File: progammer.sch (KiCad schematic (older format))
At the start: 75 parts, among them J5 USB_B_Micro, U1 ICE40HX4K-TQ144, U11 SN74LVC2T45DCUR, U13 SN74AXC4T245PWR, U14 MIC5365-3.3YC5, U16 SN74LVC2T45DCUR, U17 SN74LVC2T45DCUR, U18 SN74LVC2T45DCUR, U19 SN74LVC2T45DCUR, U3 93LCxxBT-I_OT, U4 FT2232H, U5 IS25LP080D, Y1 ECS-3225S33-120-FN-TR

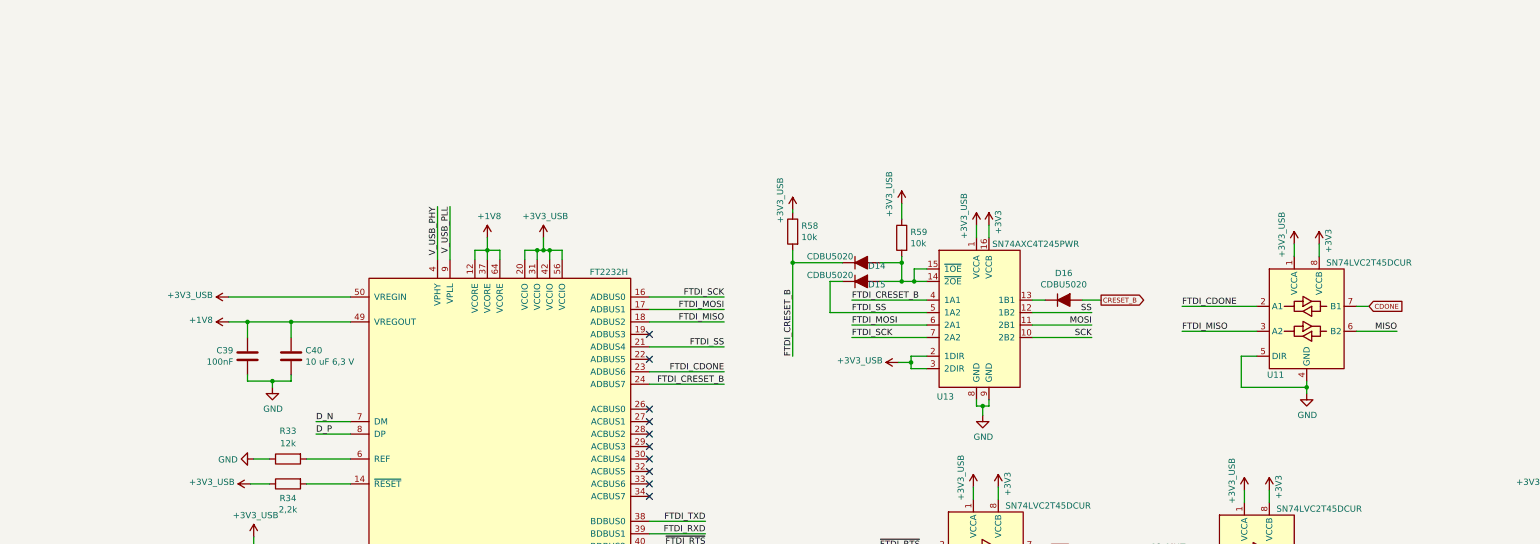
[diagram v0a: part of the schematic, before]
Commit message: Changed power isolation to usb power to use an open drain translator for the reset signals. Continued on routing
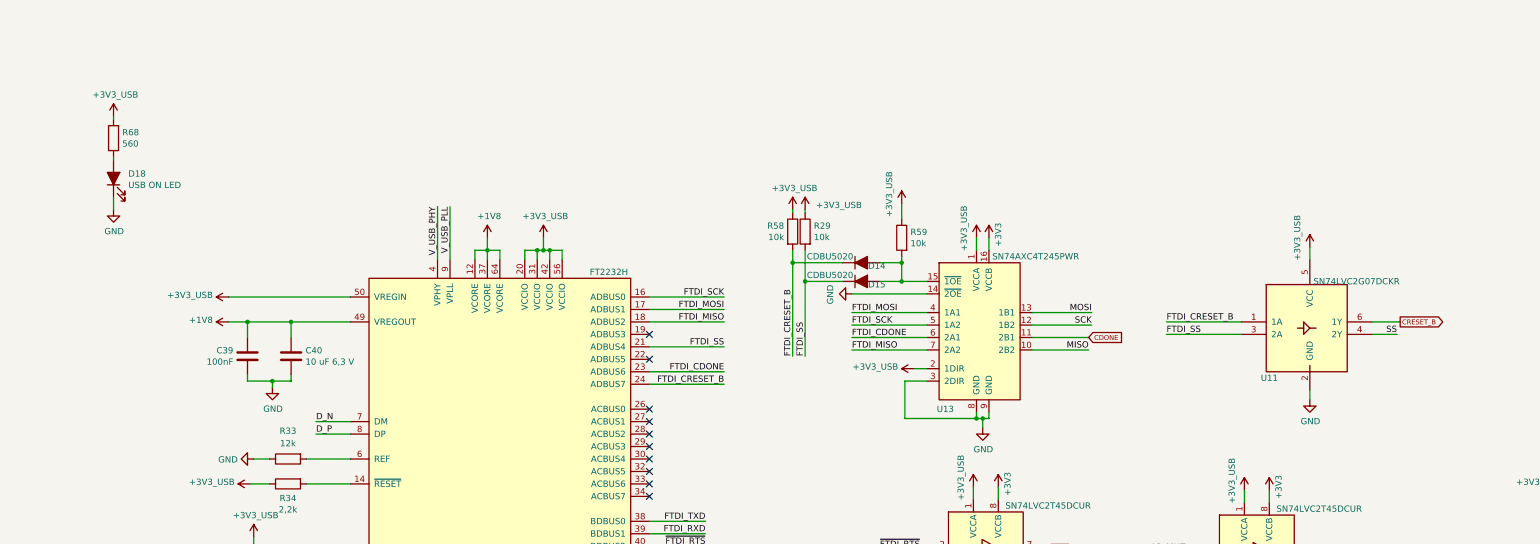
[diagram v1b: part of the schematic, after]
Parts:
- removed D16: CDBU5020, Diode_SMD:D_0603_1608Metric, symbol Device:D_ALT
- removed U11: SN74LVC2T45DCUR, Package_SO:VSSOP-8_2.4x2.1mm_P0.5mm, symbol Logic_LevelTranslator:SN74LVC2T45DCUR
- added D18: USB ON LED, LED_SMD:LED_0603_1608Metric, symbol Device:LED_ALT
- added R29: 10k, Resistor_SMD:R_0603_1608Metric, symbol Device:R
- added R68: 560, Resistor_SMD:R_0603_1608Metric, symbol Device:R
- added U11: SN74LVC2G07DCKR, Package_TO_SOT_SMD:SOT-363_SC-70-6, symbol SN74LVC2G07:SN74LVC2G07DCKR
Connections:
- net +3V3_FTDI: now also R29.1, R68.1, U11.5 (VCC); no longer U13.3 (2DIR)
- net CDONE: now also U13.11 (2B1)
- net CRESET_B: now also U11.6 (1Y)
- net FTDI_CDONE: now also U13.6 (2A1)
- net FTDI_CRESET_B: now also U11.1 (1A); no longer U13.4 (1A1)
- net FTDI_MISO: now also U13.7 (2A2)
- net FTDI_MOSI: now also U13.4 (1A1); no longer U13.6 (2A1)
- net FTDI_SCK: now also U13.5 (1A2); no longer U13.7 (2A2)
- net FTDI_SS: now also R29.2, U11.3 (2A); no longer U13.5 (1A2)
- net GND: now also U13.14 (~2OE~), U13.3 (2DIR), D18.1 (K), U11.2 (GND)
- net MISO: now also U13.10 (2B2)
- net MOSI: now also U13.13 (1B1); no longer U13.11 (2B1)
- net SCK: now also U13.12 (1B2); no longer U13.10 (2B2)
- net SS: now also U11.4 (2Y); no longer U13.12 (1B2)
- net at D14.2 (A), D15.2 (A), R59.2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: no longer U13.14 (~2OE~)
- new net: D18.2 (A), R68.2
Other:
- moved on the sheet: U13

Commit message: Routing mostly done
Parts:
- removed C80: 100nF, Capacitor_SMD:C_0603_1608Metric, symbol Device:C
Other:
- moved on the sheet: C79
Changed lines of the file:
@@
 L Device:C C?
 U 1 1 60913933
-P 8425 10350
+P 9050 10350
 AR Path="/5CAB7CD4/60913933" Ref="C?"  Part="1"
 AR Path="/5CAB8B22/60913933" Ref="C79"  Part="1"
-F 0 "C79" H 8311 10396 50  0000 R CNN
-F 1 "100nF" H 8311 10305 50  0000 R CNN
-F 2 "Capacitor_SMD:C_0603_1608Metric" H 8463 10200 50  0001 C CNN
-F 3 "~" H 8425 10350 50  0001 C CNN
-	1    8425 10350
-	1    0    0    -1
-$EndComp
-$Comp
-L Device:C C?
-U 1 1 6091393D
-P 8775 10350
-AR Path="/5CAB7CD4/6091393D" Ref="C?"  Part="1"
-AR Path="/5CAB8B22/6091393D" Ref="C80"  Part="1"
-F 0 "C80" H 8890 10396 50  0000 L CNN
-F 1 "100nF" H 8890 10305 50  0000 L CNN
-F 2 "Capacitor_SMD:C_0603_1608Metric" H 8813 10200 50  0001 C CNN
-F 3 "~" H 8775 10350 50  0001 C CNN
-	1    8775 10350
-	1    0    0    -1
-$EndComp
-Wire Wire Line
-	8425 10200 8425 10150
-Wire Wire Line
-	8425 10150 8775 10150
+F 0 "C79" H 8936 10396 50  0000 R CNN
+F 1 "100nF" H 8936 10305 50  0000 R CNN
+F 2 "Capacitor_SMD:C_0603_1608Metric" H 9088 10200 50  0001 C CNN
+F 3 "~" H 9050 10350 50  0001 C CNN
+	1    9050 10350
+	1    0    0    -1
+$EndComp
+Wire Wire Line
+	9050 10200 9050 10150
 Connection ~ 9525 10150
 Wire Wire Line
-	8775 10200 8775 10150
-Connection ~ 8775 10150
-Wire Wire Line
-	8775 10150 9525 10150
-Wire Wire Line
-	8425 10500 8425 10575
-Wire Wire Line
-	8425 10575 8775 10575
+	9050 10500 9050 10575
 Connection ~ 9525 10575
-Wire Wire Line
-	8775 10500 8775 10575
-Connection ~ 8775 10575
-Wire Wire Line
-	8775 10575 9525 10575
 Wire Notes Line
 	11400 9875 11400 10925
@@
 	1    0    0    -1
 $EndComp
+Wire Wire Line
+	9050 10150 9525 10150
+Wire Wire Line
+	9050 10575 9525 10575
 $EndSCHEMATC

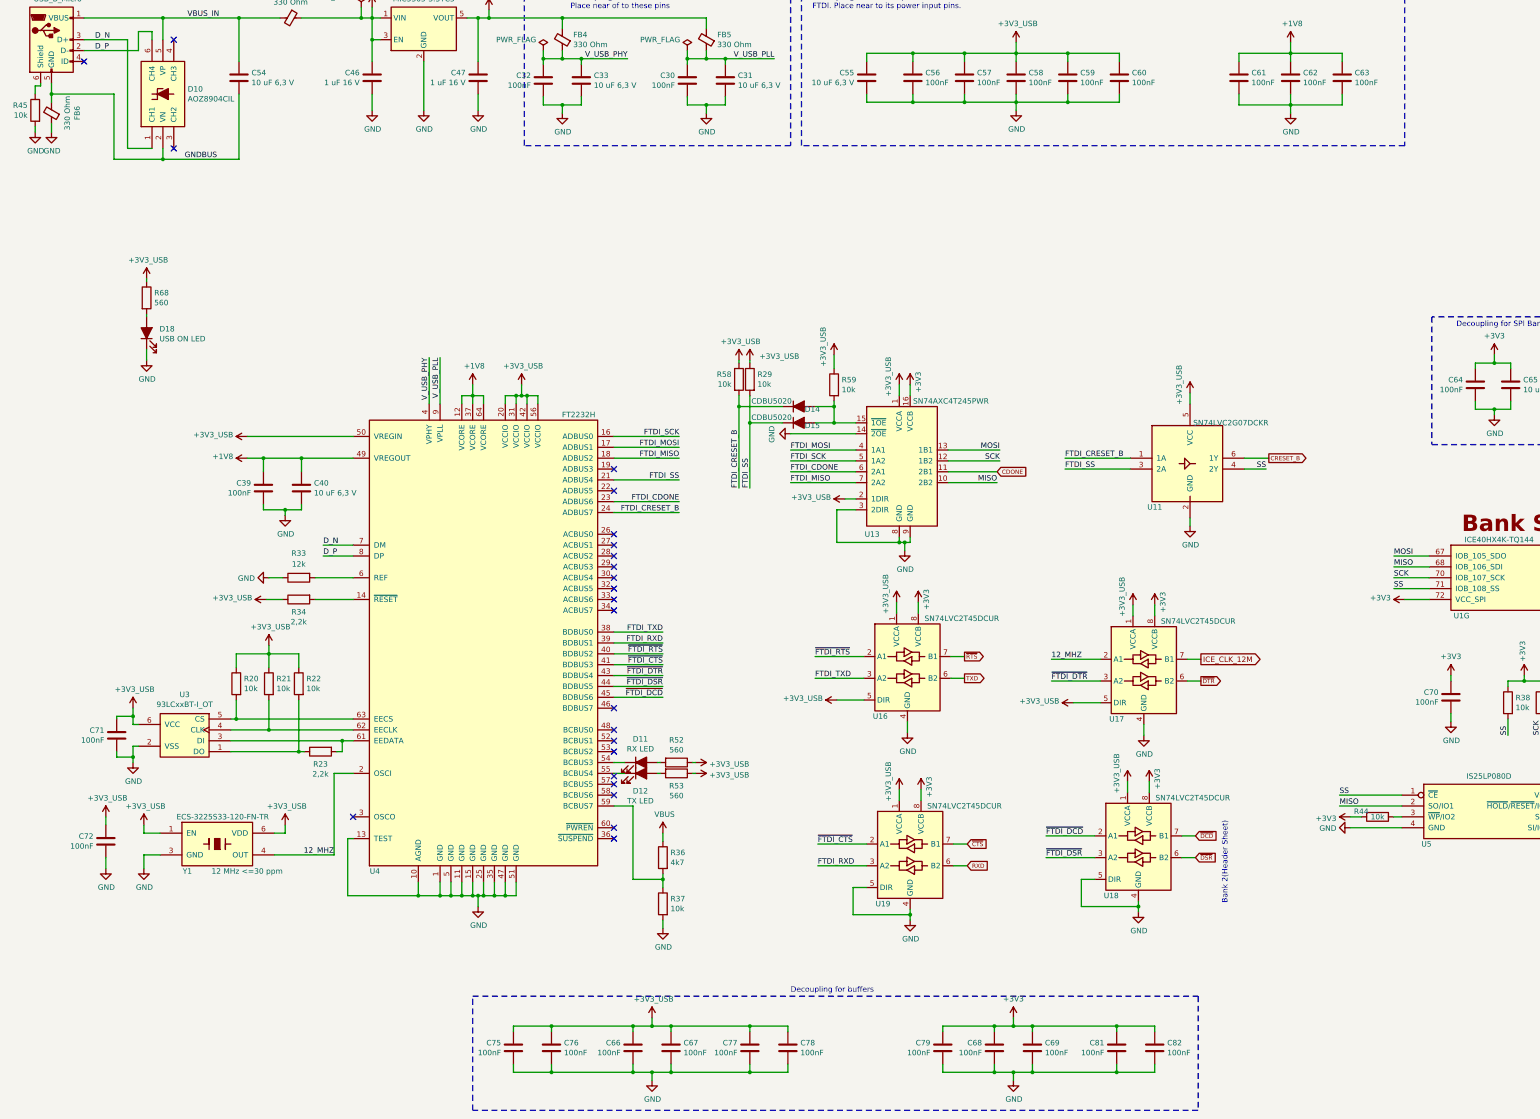
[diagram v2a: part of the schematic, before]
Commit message: Added more BOM information, updated fpga symbol, added some more 3d models
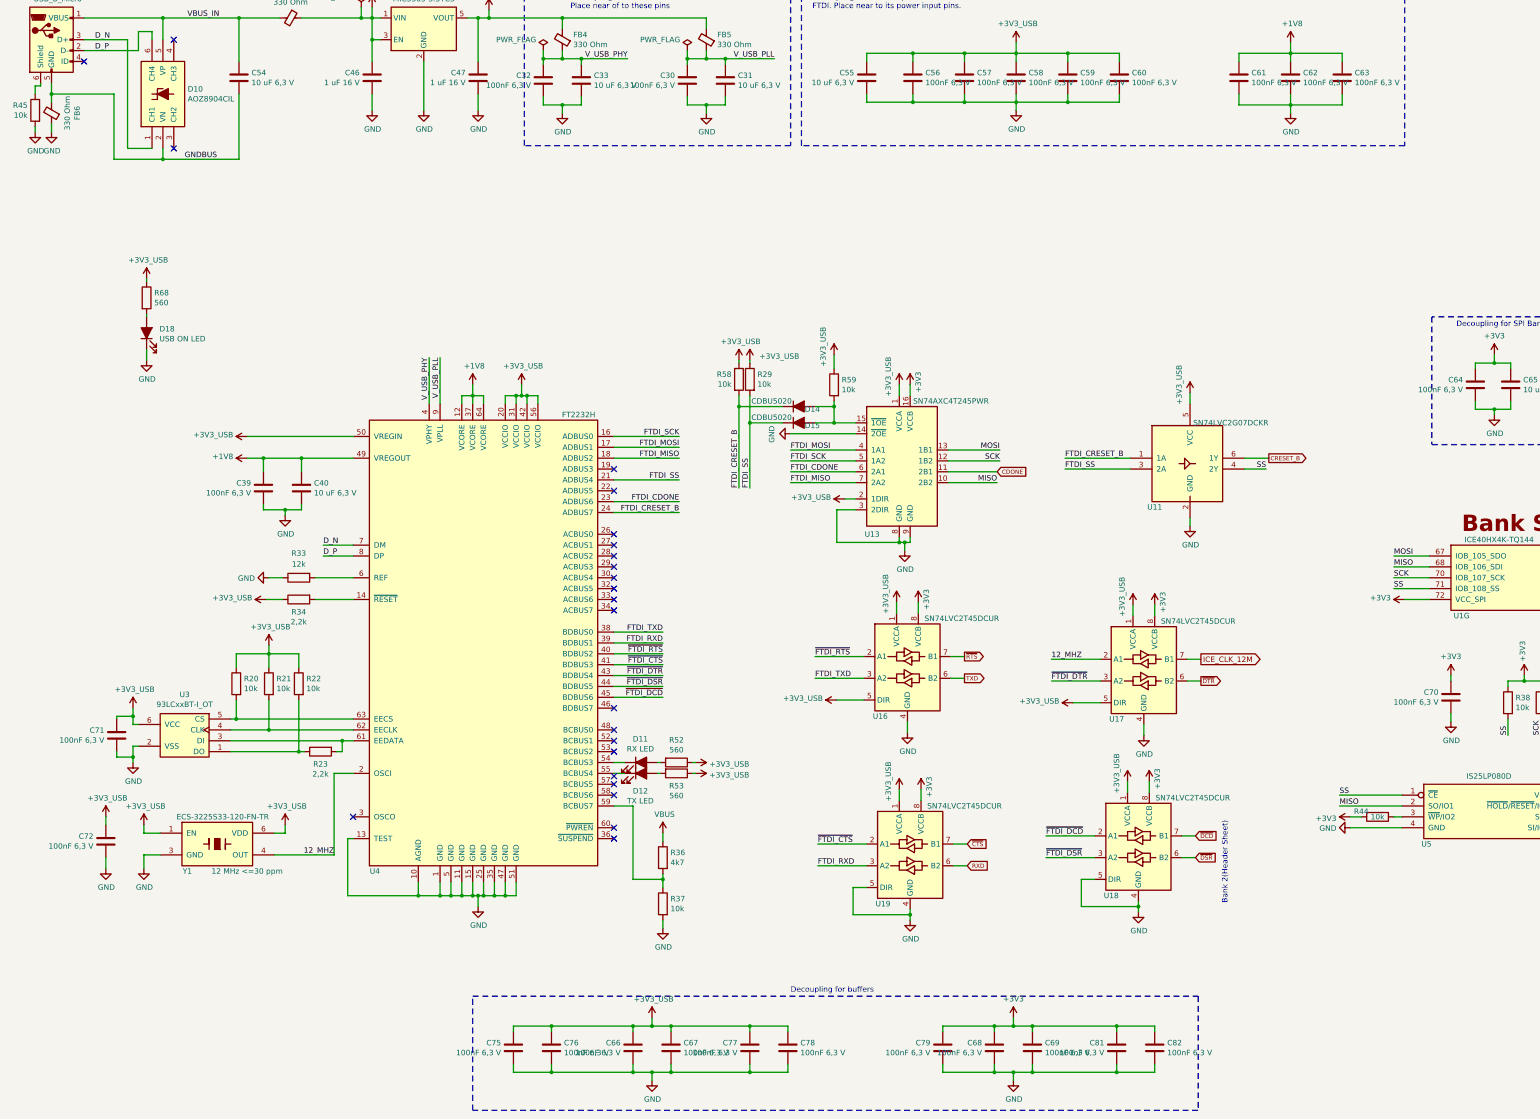
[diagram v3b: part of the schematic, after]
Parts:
- C30, C32, C39, C56, C57, C58, C59, C60, C61, C62, C63, C64, C66, C67, C68, C69, C70, C71, C72, C75, C76, C77, C78, C79, C81, C82: value 100nF -> 100nF 6,3 V; Description (none) -> CAP CER 0.1UF 50V X7R 0603; Digikey (none) -> 1276-1000-1-ND; Mfg Name (none) -> Samsung Electro-Mechanics; Mfg Part Num (none) -> CL10B104KB8NNNC; Spec (none) -> Any
- C31, C33, C40, C46, C47, C54, C55, C65, D14, D15: Spec (none) -> Any
- D10, FB3, FB4, FB5, FB6, J5, U11, U16, U17, U18, U19, Y1: Spec (none) -> Spec
- U1: Description (none) -> IC FPGA 107 I/O 144TQFP; Digikey (none) -> 220-1572-ND; Mfg Name (none) -> Lattice Semiconductor Corporation; Mfg Part Num (none) -> ICE40HX4K-TQ144; Spec (none) -> Spec
- U13: Description (none) -> LOGIC GATES AND INVERTERS; Digikey (none) -> 296-53472-1-ND; Mfg Name (none) -> Texas Instruments; Mfg Part Num (none) -> SN74AXC4T245PWR; Spec (none) -> Spec
- U14: Description (none) -> IC REG LINEAR 3.3V 150MA SC70-5; Digikey (none) -> 576-3193-1-ND; Mfg Name (none) -> Microchip Technology; Mfg Part Num (none) -> MIC5365-3.3YC5-TR; Spec (none) -> Spec
- U3: Description (none) -> IC EEPROM 2K SPI 2MHZ SOT23-6; Digikey (none) -> 93LC56BT-I/OTCT-ND; Mfg Name (none) -> Microchip Technology; Mfg Part Num (none) -> 93LC56BT-I/OT; Spec (none) -> Spec
- U4: Description (none) -> IC USB HS DUAL UART/FIFO 64-LQFP; Digikey (none) -> 768-1024-1-ND; Mfg Name (none) -> FTDI, Future Technology Devices International Ltd; Mfg Part Num (none) -> FT2232HL-REEL; Spec (none) -> Spec
- U5: Description (none) -> IC FLASH 8M SPI 133MHZ 8SOP; Digikey (none) -> 706-1580-ND; Mfg Name (none) -> ISSI, Integrated Silicon Solution Inc; Mfg Part Num (none) -> IS25LP080D-JNLE; Spec (none) -> Spec

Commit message: Corrected a few footprints
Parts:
- Y1: footprint footprints:ECS-3225S_3.2x2.5mm_footprint -> footprints:Y_ECS-3225S_3.2x2.5mm_footprint
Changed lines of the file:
@@
 F 0 "Y1" H 2100 8225 50  0000 C CNN
 F 1 "ECS-3225S33-120-FN-TR" H 2425 8725 50  0000 C CNN
-F 2 "footprints:ECS-3225S_3.2x2.5mm_footprint" H 2400 7875 50  0001 C CNN
+F 2 "footprints:Y_ECS-3225S_3.2x2.5mm_footprint" H 2400 7875 50  0001 C CNN
 F 3 "https://www.ecsxtal.com/store/pdf/ECS-3225S.pdf" H 2400 7875 50  0001 C CNN
 F 4 "ECS Inc." H 2400 8475 50  0001 C CNN "Mfg Name"
